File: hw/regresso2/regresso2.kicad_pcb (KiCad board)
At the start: 2 copper layers, 48.9 x 53.3 mm, 37 parts, among them CN5 Conn_01x10, CN6 Conn_01x08, CN8 Conn_01x06, CN9 Conn_01x08, J1 CONN_01X02, P10 CONTROL, P9 FX2LA, U1 STM32F303CCTx, U2 MIC550x-3.3YM5, Y1 Crystal_GND24_Small

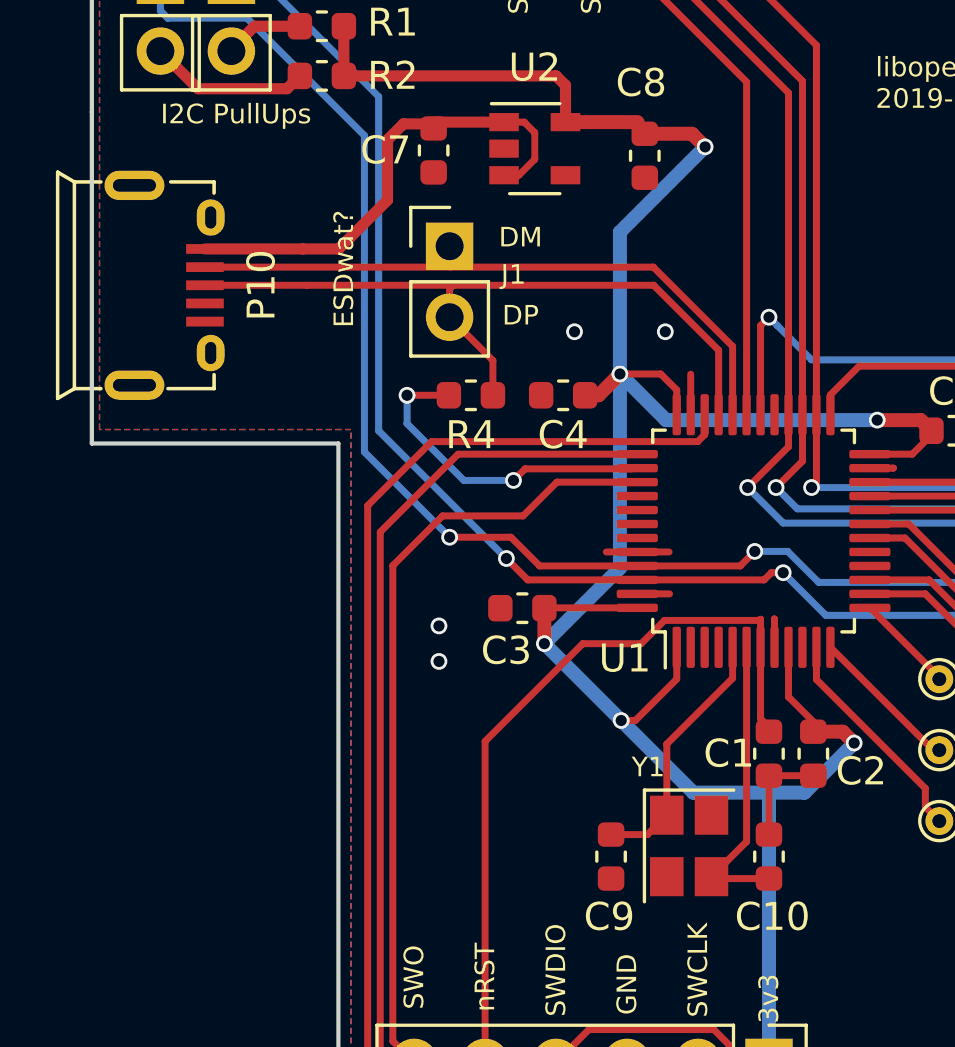
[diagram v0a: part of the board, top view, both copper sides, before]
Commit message: hw/regresso2: restore stock parts for hand soldering
getting seeed to assembly still isn't really all that cheap, so put back
the parts I have on hand for doing my own assembly
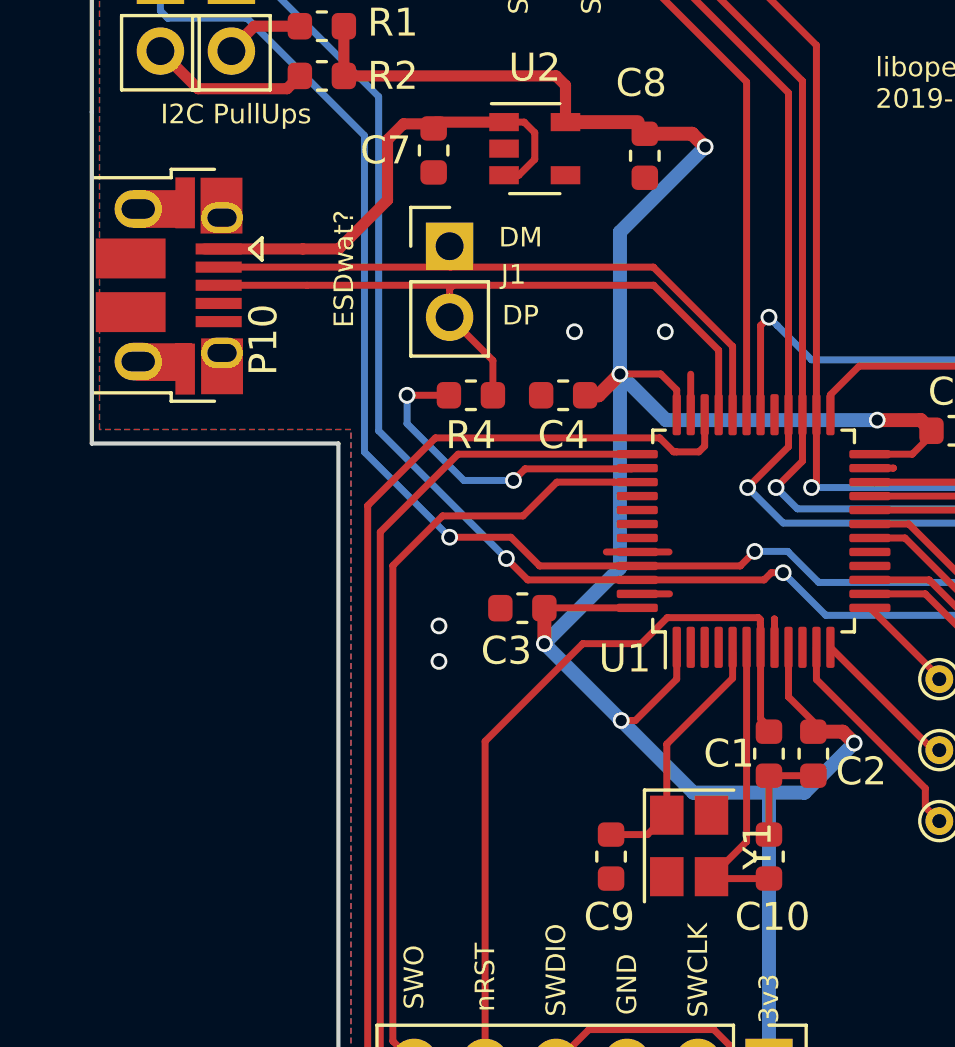
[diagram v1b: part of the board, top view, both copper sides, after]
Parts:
- C10, C9: value 18pf -> 12pf
- P10: footprint OPL_Connector:MICRO-USB5+6P-SMD-0.65-AB -> Connector_USB:USB_Micro-B_Amphenol_10103594-0001LF_Horizontal
- Y1: footprint Crystals:Crystal_SMD_SeikoEpson_FA238-4pin_3.2x2.5mm -> Crystal:Crystal_SMD_SeikoEpson_FA238-4Pin_3.2x2.5mm
- moved P10 1.25 mm to (130.9, 92.2)
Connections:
- P10 pad 6: (no net) -> Net-(P10-Pad6)
